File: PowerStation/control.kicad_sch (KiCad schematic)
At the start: 1 part

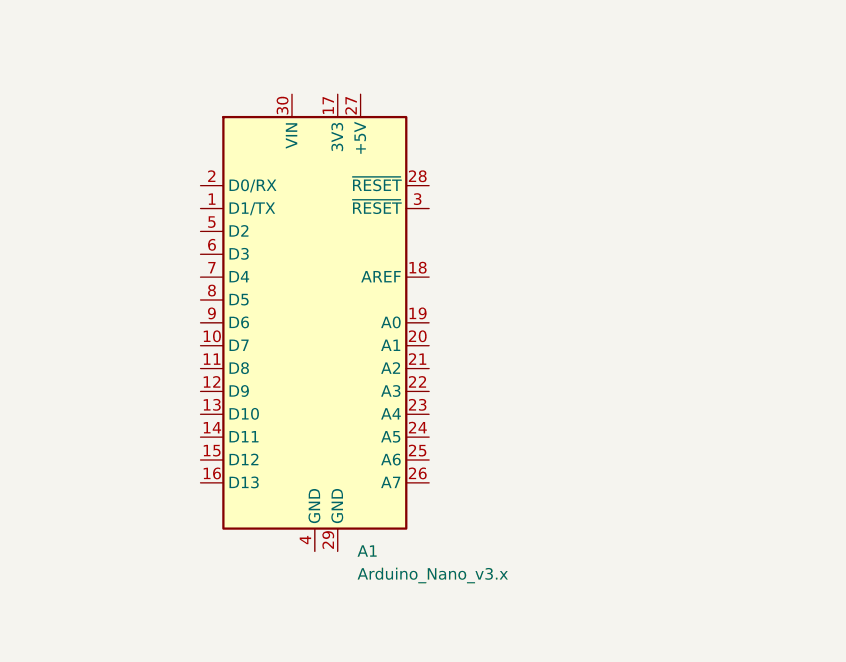
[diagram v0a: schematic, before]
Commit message: terminando diagrama
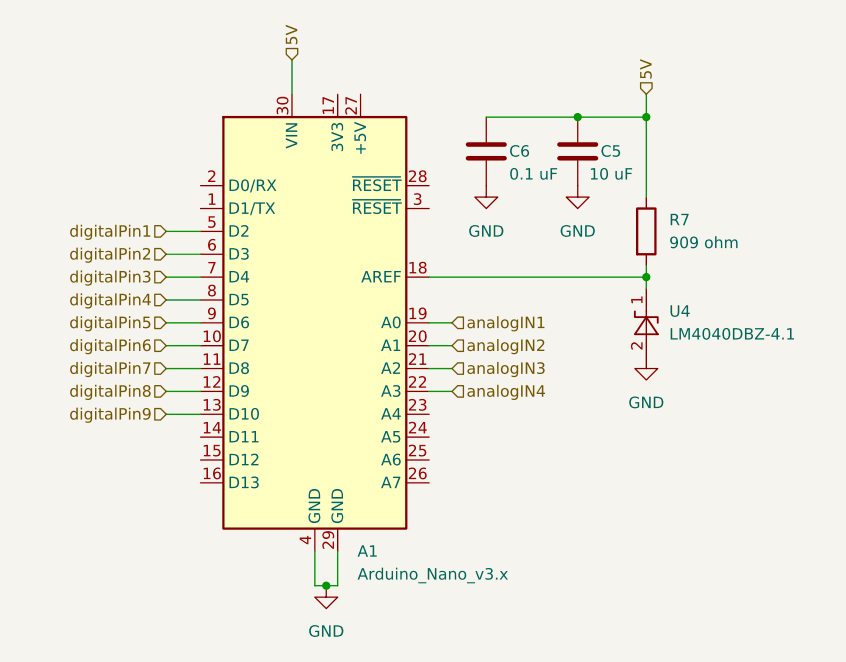
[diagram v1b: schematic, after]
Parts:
- added C5: 10 uF, symbol Device:C
- added C6: 0.1 uF, symbol Device:C
- added R7: 909 ohm, symbol Device:R
- added U4: LM4040DBZ-4.1, Package_TO_SOT_SMD:SOT-23, symbol Reference_Voltage:LM4040DBZ-4.1
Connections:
- net digitalPin6: now reaches A1.10 (D7)
- net digitalPin7: now reaches A1.11 (D8)
- net digitalPin8: now reaches A1.12 (D9)
- net digitalPin9: now reaches A1.13 (D10)
- net at A1.18 (AREF): now also R7.2, U4.1 (K)
- net analogIN1: now reaches A1.19 (A0)
- net analogIN2: now reaches A1.20 (A1)
- net analogIN3: now reaches A1.21 (A2)
- net analogIN4: now reaches A1.22 (A3)
- net GND: now reaches A1.29 (GND)
- net GND: now also A1.4 (GND), C5.2, C6.2, U4.2 (A)
- net 5V: now reaches A1.30 (VIN)
- net 5V: now also C5.1, C6.1, R7.1
- net digitalPin1: now reaches A1.5 (D2)
- net digitalPin2: now reaches A1.6 (D3)
- net digitalPin3: now reaches A1.7 (D4)
- net digitalPin4: now reaches A1.8 (D5)
- net digitalPin5: now reaches A1.9 (D6)

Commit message: avanxe en placa
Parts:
- C5, C6: footprint (none) -> Capacitor_SMD:C_0402_1005Metric
- R7: footprint (none) -> Resistor_SMD:R_0402_1005Metric
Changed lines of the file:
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@@
       (effects (font (size 1.27 1.27)) (justify left))
     )
-    (property "Footprint" "" (at 154.6352 66.04 0)
+    (property "Footprint" "Capacitor_SMD:C_0402_1005Metric" (at 154.6352 66.04 0)
       (effects (font (size 1.27 1.27)) hide)
     )
@@
       (effects (font (size 1.27 1.27)) (justify left))
     )
-    (property "Footprint" "" (at 159.512 71.12 90)
+    (property "Footprint" "Resistor_SMD:R_0402_1005Metric" (at 159.512 71.12 90)
       (effects (font (size 1.27 1.27)) hide)
     )
@@
       (effects (font (size 1.27 1.27)) (justify left))
     )
-    (property "Footprint" "" (at 144.4752 66.04 0)
+    (property "Footprint" "Capacitor_SMD:C_0402_1005Metric" (at 142.24 50.8 0)
       (effects (font (size 1.27 1.27)) hide)
     )

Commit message: correccion de esquermatico y avanze en placa
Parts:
- renumbered C6 to C1, C5 to C2, R7 to R1, U4 to U1
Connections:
- net AREF: now reaches A1.18 (AREF), R1.2, U1.1 (K)
- net digitalPin10: now reaches A1.14 (D11)
- net digitalPin11: now reaches A1.15 (D12)
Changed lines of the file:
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@@
+    (stroke (width 0) (type default))
+  )
+  (wire (pts (xy 108.204 93.98) (xy 111.76 93.98))
     (stroke (width 0) (type default))
   )
@@
     (stroke (width 0) (type default))
   )
+  (wire (pts (xy 108.204 96.52) (xy 111.76 96.52))
+    (stroke (width 0) (type default))
+  )
   (wire (pts (xy 107.95 73.66) (xy 111.76 73.66))
     (stroke (width 0) (type default))
@@
     (stroke (width 0) (type default))
   )
+  (label "AREF" (at 146.558 76.2 0) (fields_autoplaced)
+    (effects (font (size 1.27 1.27)) (justify left bottom))
+  )
   (hierarchical_label "5V" (shape input) (at 121.92 52.07 90) (fields_autoplaced)
     (effects (font (size 1.27 1.27)) (justify left))
@@
     (effects (font (size 1.27 1.27)) (justify right))
   )
+  (hierarchical_label "digitalPin11" (shape input) (at 108.204 96.52 180) (fields_autoplaced)
+    (effects (font (size 1.27 1.27)) (justify right))
+  )
   (hierarchical_label "analogIN3" (shape input) (at 139.7 86.36 0) (fields_autoplaced)
     (effects (font (size 1.27 1.27)) (justify left))
@@
     (effects (font (size 1.27 1.27)) (justify right))
   )
+  (hierarchical_label "digitalPin10" (shape input) (at 108.204 93.98 180) (fields_autoplaced)
+    (effects (font (size 1.27 1.27)) (justify right))
+  )
   (hierarchical_label "digitalPin1" (shape input) (at 107.95 71.12 180) (fields_autoplaced)
     (effects (font (size 1.27 1.27)) (justify right))
@@
   (symbol (lib_id "power:GND") (at 153.67 66.04 0) (unit 1)
     (in_bom yes) (on_board yes) (dnp no) (fields_autoplaced)
-    (property "Reference" "#PWR019" (at 153.67 72.39 0)
+    (property "Reference" "#PWR07" (at 153.67 72.39 0)
       (effects (font (size 1.27 1.27)) hide)
     )
@@
       (project "PowerStation"
         (path "/b9c1e1ca-72f8-499b-86c1-59e3d070e292/d71487c1-0901-43ff-b529-103a258ba6bc"
-          (reference "#PWR019") (unit 1)
+          (reference "#PWR07") (unit 1)
         )
       )
@@
   (symbol (lib_id "Device:C") (at 153.67 62.23 0) (unit 1)
     (in_bom yes) (on_board yes) (dnp no)
-    (property "Reference" "C5" (at 156.21 62.23 0)
+    (property "Reference" "C2" (at 156.21 62.23 0)
       (effects (font (size 1.27 1.27)) (justify left))
     )
@@
       (project "PowerStation"
         (path "/b9c1e1ca-72f8-499b-86c1-59e3d070e292/d71487c1-0901-43ff-b529-103a258ba6bc"
-          (reference "C5") (unit 1)
+          (reference "C2") (unit 1)
         )
       )
@@
   (symbol (lib_id "Device:R") (at 161.29 71.12 0) (unit 1)
     (in_bom yes) (on_board yes) (dnp no) (fields_autoplaced)
-    (property "Reference" "R7" (at 163.83 69.85 0)
+    (property "Reference" "R1" (at 163.83 69.85 0)
       (effects (font (size 1.27 1.27)) (justify left))
     )
@@
       (project "PowerStation"
         (path "/b9c1e1ca-72f8-499b-86c1-59e3d070e292/d71487c1-0901-43ff-b529-103a258ba6bc"
-          (reference "R7") (unit 1)
+          (reference "R1") (unit 1)
         )
       )
@@
   (symbol (lib_id "power:GND") (at 161.29 85.09 0) (unit 1)
     (in_bom yes) (on_board yes) (dnp no) (fields_autoplaced)
-    (property "Reference" "#PWR018" (at 161.29 91.44 0)
+    (property "Reference" "#PWR08" (at 161.29 91.44 0)
       (effects (font (size 1.27 1.27)) hide)
     )
@@
       (project "PowerStation"
         (path "/b9c1e1ca-72f8-499b-86c1-59e3d070e292/d71487c1-0901-43ff-b529-103a258ba6bc"
-          (reference "#PWR018") (unit 1)
+          (reference "#PWR08") (unit 1)
         )
       )
@@
   (symbol (lib_id "power:GND") (at 143.51 66.04 0) (unit 1)
     (in_bom yes) (on_board yes) (dnp no) (fields_autoplaced)
-    (property "Reference" "#PWR020" (at 143.51 72.39 0)
+    (property "Reference" "#PWR06" (at 143.51 72.39 0)
       (effects (font (size 1.27 1.27)) hide)
     )
@@
       (project "PowerStation"
         (path "/b9c1e1ca-72f8-499b-86c1-59e3d070e292/d71487c1-0901-43ff-b529-103a258ba6bc"
-          (reference "#PWR020") (unit 1)
+          (reference "#PWR06") (unit 1)
         )
       )
@@
   (symbol (lib_id "Device:C") (at 143.51 62.23 0) (unit 1)
     (in_bom yes) (on_board yes) (dnp no)
-    (property "Reference" "C6" (at 146.05 62.23 0)
+    (property "Reference" "C1" (at 146.05 62.23 0)
       (effects (font (size 1.27 1.27)) (justify left))
     )
@@
       (project "PowerStation"
         (path "/b9c1e1ca-72f8-499b-86c1-59e3d070e292/d71487c1-0901-43ff-b529-103a258ba6bc"
-          (reference "C6") (unit 1)
+          (reference "C1") (unit 1)
         )
       )
@@
   (symbol (lib_id "Reference_Voltage:LM4040DBZ-4.1") (at 161.29 81.28 90) (unit 1)
     (in_bom yes) (on_board yes) (dnp no) (fields_autoplaced)
-    (property "Reference" "U4" (at 163.83 80.01 90)
+    (property "Reference" "U1" (at 163.83 80.01 90)
       (effects (font (size 1.27 1.27)) (justify right))
     )
@@
       (project "PowerStation"
         (path "/b9c1e1ca-72f8-499b-86c1-59e3d070e292/d71487c1-0901-43ff-b529-103a258ba6bc"
-          (reference "U4") (unit 1)
+          (reference "U1") (unit 1)
         )
       )
@@
   (symbol (lib_id "power:GND") (at 125.73 110.49 0) (unit 1)
     (in_bom yes) (on_board yes) (dnp no) (fields_autoplaced)
-    (property "Reference" "#PWR017" (at 125.73 116.84 0)
+    (property "Reference" "#PWR09" (at 125.73 116.84 0)
       (effects (font (size 1.27 1.27)) hide)
     )
@@
       (project "PowerStation"
         (path "/b9c1e1ca-72f8-499b-86c1-59e3d070e292/d71487c1-0901-43ff-b529-103a258ba6bc"
-          (reference "#PWR017") (unit 1)
-        )
-      )
+          (reference "#PWR09") (unit 1)
+        )
+      )
